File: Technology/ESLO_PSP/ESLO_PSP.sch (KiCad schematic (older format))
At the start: 42 parts, among them J1 Imeas, P5 Digital, P6 Analog, U1 LP5907MFX-1.8, U2 LP5907MFX-1.5, U3 MAX1720, U4 TPS72301DDCT, U5 nRF24L01P, U6 AN91445, Y1 SXT21412AA16

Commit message: ESLO project updates
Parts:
- C4, C5: value 1uF -> 10uF
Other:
- note added: "NO CAP!!"
- note added: "Should this be to +1.8v for the LP5907-1.5?"
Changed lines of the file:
@@
 P 2350 2200
 F 0 "C4" V 2602 2200 50  0000 C CNN
-F 1 "1uF" V 2511 2200 50  0000 C CNN
+F 1 "10uF" V 2511 2200 50  0000 C CNN
 F 2 "Capacitor_SMD:C_0402_1005Metric" H 2388 2050 50  0001 C CNN
 F 3 "~" H 2350 2200 50  0001 C CNN
@@
 P 2850 2550
 F 0 "C5" H 2735 2504 50  0000 R CNN
-F 1 "1uF" H 2735 2595 50  0000 R CNN
+F 1 "10uF" H 2735 2595 50  0000 R CNN
 F 2 "Capacitor_SMD:C_0402_1005Metric" H 2888 2400 50  0001 C CNN
 F 3 "~" H 2850 2550 50  0001 C CNN
@@
 Wire Wire Line
 	2050 1600 2700 1600
+Text Notes 200  1450 0    50   ~ 0
+Should this be to +1.8v for the LP5907-1.5?
+Text Notes 4500 3150 0    50   ~ 0
+NO CAP!!
 $EndSCHEMATC

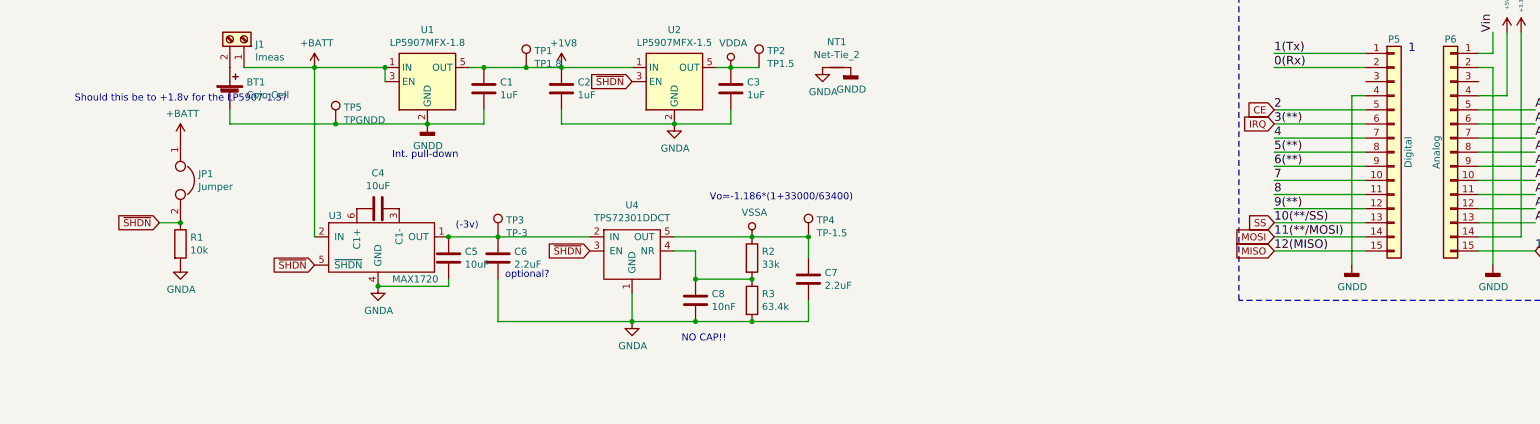
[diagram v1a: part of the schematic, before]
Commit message: Reconsidering ESLO architecture (-> CC2640R2)
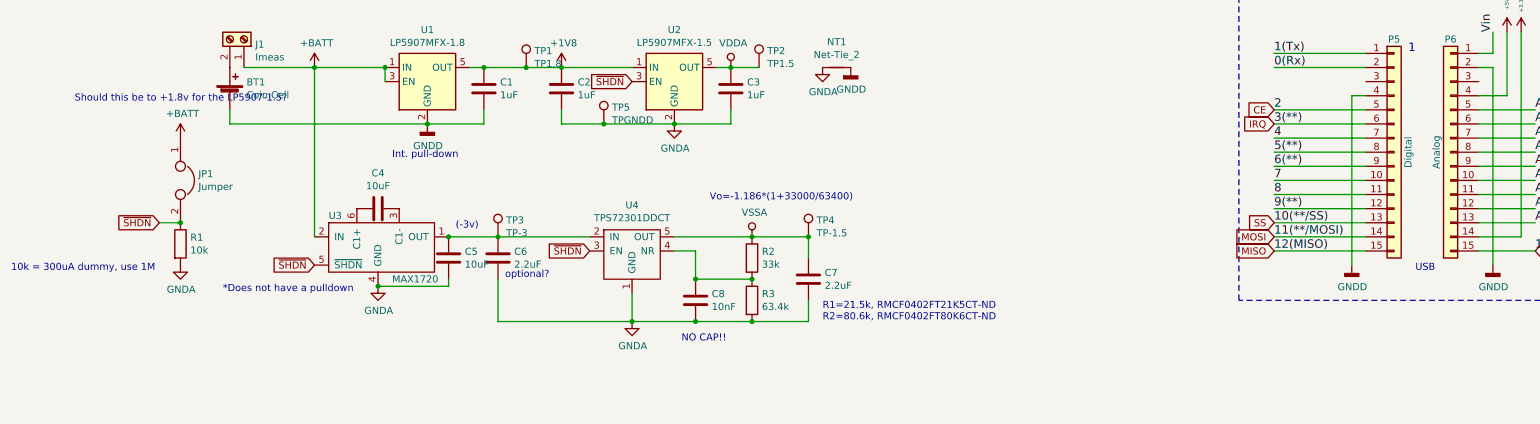
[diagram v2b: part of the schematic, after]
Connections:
- net GNDA: now also TP5.1
- net GNDD: no longer TP5.1
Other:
- note added: "*Does not have a pulldown"
- note added: "10k = 300uA dummy, use 1M"
- note added: "R1=21.5k, RMCF0402FT21K5CT-ND\nR2=80.6k, RMCF0402FT80K6CT-ND‎"
- note added: "USB"
- moved on the sheet: TP5
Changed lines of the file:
@@
 Wire Wire Line
 	1300 1500 1300 1600
-Wire Wire Line
-	1300 1600 2050 1600
 $Comp
 L ARBO_library:MAX1720 U3
@@
 	3650 1500 3650 1600
 Wire Wire Line
-	3650 1600 4450 1600
+	3650 1600 3950 1600
 Text Notes 2900 2350 0    50   ~ 0
 (-3v)\n
@@
 L Connector:TestPoint TP5
 U 1 1 5F3F265E
-P 2050 1600
-F 0 "TP5" H 2108 1718 50  0000 L CNN
-F 1 "TPGNDD" H 2108 1627 50  0000 L CNN
-F 2 "TestPoint:TestPoint_Keystone_5000-5004_Miniature" H 2250 1600 50  0001 C CNN
-F 3 "~" H 2250 1600 50  0001 C CNN
-F 4 "36-5000-ND" H 2050 1600 50  0001 C CNN "Digikey"
-	1    2050 1600
-	1    0    0    -1
-$EndComp
-Connection ~ 2050 1600
-Wire Wire Line
-	2050 1600 2700 1600
+P 3950 1600
+F 0 "TP5" H 4008 1718 50  0000 L CNN
+F 1 "TPGNDD" H 4008 1627 50  0000 L CNN
+F 2 "TestPoint:TestPoint_Keystone_5000-5004_Miniature" H 4150 1600 50  0001 C CNN
+F 3 "~" H 4150 1600 50  0001 C CNN
+F 4 "36-5000-ND" H 3950 1600 50  0001 C CNN "Digikey"
+	1    3950 1600
+	1    0    0    -1
+$EndComp
 Text Notes 200  1450 0    50   ~ 0
 Should this be to +1.8v for the LP5907-1.5?
 Text Notes 4500 3150 0    50   ~ 0
 NO CAP!!
+Connection ~ 3950 1600
+Wire Wire Line
+	3950 1600 4450 1600
+Wire Wire Line
+	1300 1600 2700 1600
+Text Notes 1250 2800 0    50   ~ 0
+*Does not have a pulldown
+Text Notes -250 2650 0    50   ~ 0
+10k = 300uA dummy, use 1M
+Text Notes 9700 2650 0    50   ~ 0
+USB
+Text Notes 5500 3000 0    50   ~ 0
+R1=21.5k, RMCF0402FT21K5CT-ND\nR2=80.6k, RMCF0402FT80K6CT-ND‎
 $EndSCHEMATC
